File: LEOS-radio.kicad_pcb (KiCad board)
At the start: 2 copper layers, 100 x 100 mm, 20 parts, among them J1 MicroFit_1x4, J2 MicroFit_1x4, U1 MCP2562FD, U2 MCP2518FD, U3 E22-900M30S, Y1 40 MHz

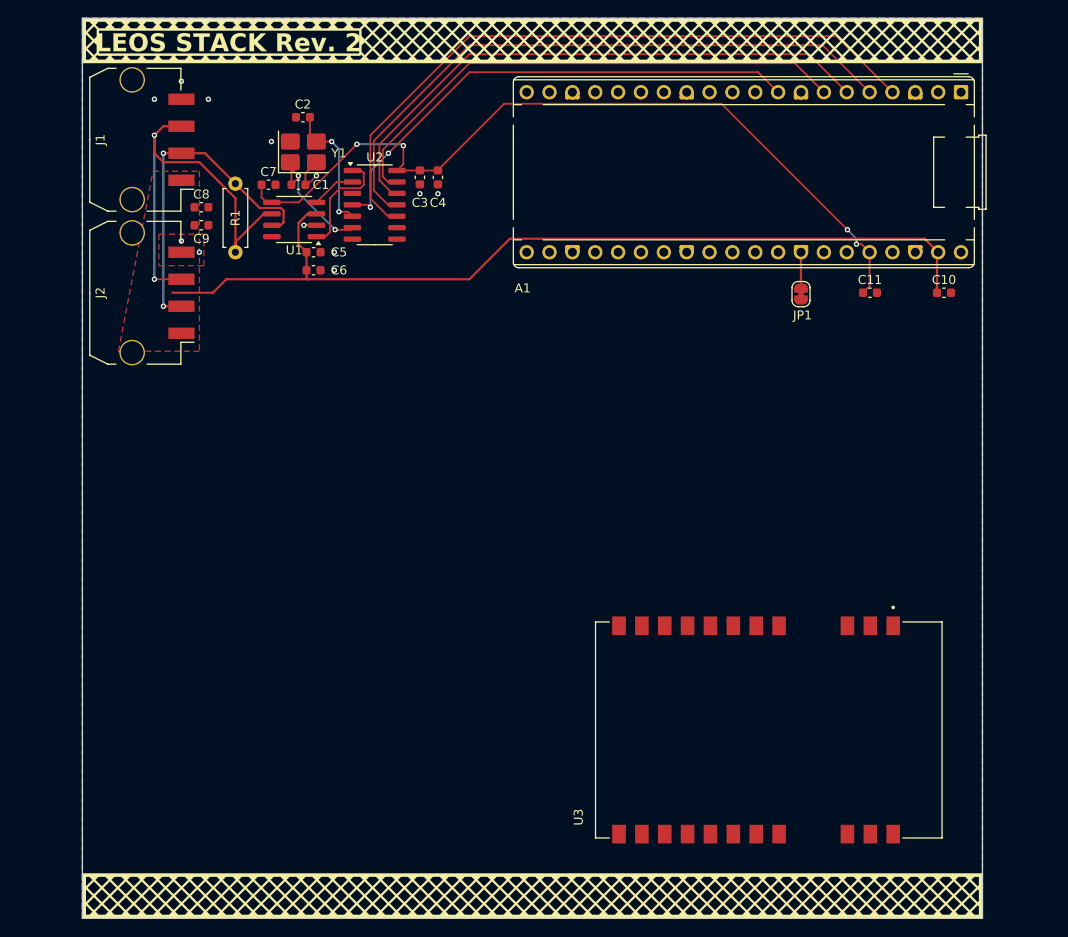
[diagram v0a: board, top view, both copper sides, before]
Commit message: v2 with dual 1W LoRa transcievers, edge-mount SMA connectors, and an all new design
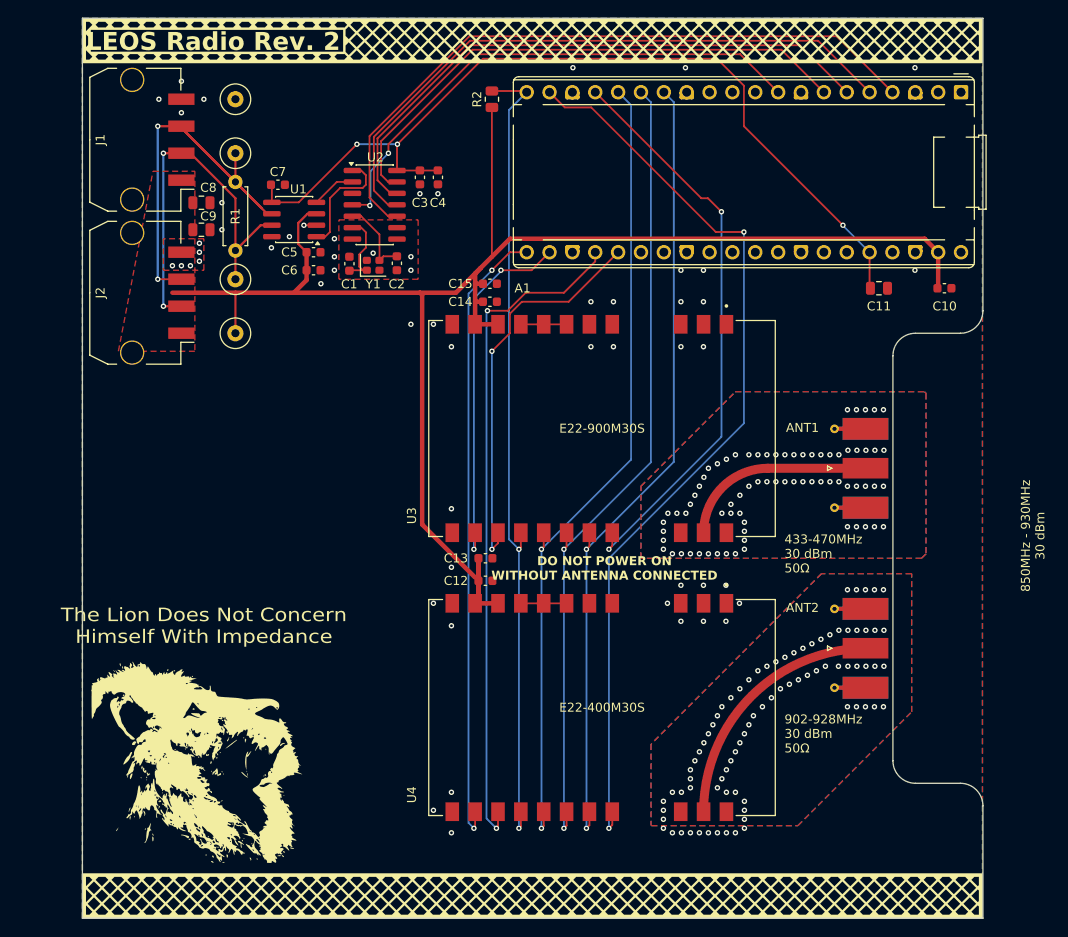
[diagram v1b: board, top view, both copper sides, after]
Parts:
- removed JP1: AGND Tie, Jumper:SolderJumper-2_P1.3mm_Bridged_RoundedPad1.0x1.5mm
- added ANT1: 900Mhz SMA, Connector_Coaxial:SMA_Molex_73251-1153_EdgeMount_Horizontal, F.Cu at (185.3, 100.0)
- added ANT2: 400MHz SMA, Connector_Coaxial:SMA_Molex_73251-1153_EdgeMount_Horizontal, F.Cu at (185.3, 120.0)
- added C12: 0.1u, Capacitor_SMD:C_0603_1608Metric, F.Cu at (144.8, 112.5)
- added C13: 1u, Capacitor_SMD:C_0603_1608Metric, F.Cu at (144.8, 110.0)
- added C14: 0.1u, Capacitor_SMD:C_0603_1608Metric, F.Cu at (145.3, 81.5)
- added C15: 1u, Capacitor_SMD:C_0603_1608Metric, F.Cu at (145.3, 79.5)
- added R2: 10k, Resistor_SMD:R_0805_2012Metric, F.Cu at (145.5, 59.0)
- added TP1: CAN-H Test Point, TestPoint:TestPoint_Loop_D2.60mm_Drill0.9mm_Beaded, F.Cu at (117.0, 79.0)
- added TP2: CAN-L Test Point, TestPoint:TestPoint_Loop_D2.60mm_Drill0.9mm_Beaded, F.Cu at (117.0, 65.0)
- added TP3: 5V Test Point, TestPoint:TestPoint_Loop_D2.60mm_Drill0.9mm_Beaded, F.Cu at (117.0, 85.0)
- added TP4: GND Test Point, TestPoint:TestPoint_Loop_D2.60mm_Drill0.9mm_Beaded, F.Cu at (117.0, 59.0)
- added U4: E22-400M30S, LEOS:XCVR_E22-900M30S, F.Cu at (157.7, 126.6)
- A1: value RaspberryPi_Pico -> RaspberryPi Pico
- C1, C2: value 12pF -> 10p
- C10, C3, C5, C7: value 0.1uF -> 0.1u
- C11: value 10uF -> 10u; footprint Capacitor_SMD:C_0603_1608Metric -> Capacitor_SMD:C_0805_2012Metric
- C4, C6: value 1uF -> 1u
- C8: value 47uF -> 22u; footprint Capacitor_SMD:C_0603_1608Metric -> Capacitor_SMD:C_0805_2012Metric
- C9: value 0.1uF -> 22u; footprint Capacitor_SMD:C_0603_1608Metric -> Capacitor_SMD:C_0805_2012Metric
- J1, J2: footprint Connector_Molex:Molex_Micro-Fit_3.0_43650-0410_1x04-1MP_P3.00mm_Horizontal_PnP -> LEOS:Molex_MicroFit3.0_43650-0410_1x04_Horizontal
- R1: value 120R -> 120
- Y1: footprint Crystal:Crystal_SMD_3225-4Pin_3.2x2.5mm_HandSoldering -> Crystal:Crystal_SMD_2016-4Pin_2.0x1.6mm
- moved U3 38.3 mm to (157.7, 95.6)
- moved C2 19.3 mm to (134.9, 77.2), turned to 90 degrees
- moved Y1 14.8 mm to (132.3, 77.5)
- moved C1 10.4 mm to (129.7, 77.3), turned to -90 degrees
- moved R1 7.81 mm to (117.0, 68.2), turned to -90 degrees
- moved C11 1.12 mm to (188.5, 80.0)
- moved C7 1.04 mm to (121.7, 68.5)
- moved C10 0.50 mm to (195.8, 80.0)
- moved C8 0.50 mm to (113.2, 70.5)
- moved C9 0.50 mm to (113.2, 73.5)
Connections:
- net /CAN+ renamed /CANbus/CAN+
- net /CAN- renamed /CANbus/CAN-
- net /CAN_CS renamed /CANbus/CS
- net /CAN_INT renamed /CANbus/INT
- net /CAN_MISO renamed /CANbus/MISO
- net /CAN_MOSI renamed /CANbus/MOSI
- net /CAN_SCK renamed /CANbus/SCK
- net /OSC2 renamed /CANbus/OSC2
- net /RXCAN renamed Net-(U1-RXD)
- net /TXCAN renamed Net-(U1-TXD)
- A1 pad 1: UART0_TX -> unconnected-(A1-GPIO0-Pad1)
- A1 pad 10: GP7 -> unconnected-(A1-GPIO7-Pad10)
- A1 pad 11: I2C0_SDA -> unconnected-(A1-GPIO8-Pad11)
- A1 pad 12: I2C0_SCL -> unconnected-(A1-GPIO9-Pad12)
- A1 pad 14: GP10 -> /RF/SCK
- A1 pad 15: GP11 -> /RF/MOSI
- A1 pad 16: GP12 -> /RF/MISO
- A1 pad 17: GP13 -> /RF/CS0
- A1 pad 19: GP14 -> /RF/CS1
- A1 pad 2: UART0_RX -> unconnected-(A1-GPIO1-Pad2)
- A1 pad 20: GP15 -> /RF/nRESET
- A1 pad 21: GP16 -> /RF/INT1
- A1 pad 22: GP17 -> /RF/INT0
- A1 pad 24: GP18 -> /RF/BUSY1
- A1 pad 25: GP19 -> /RF/BUSY0
- A1 pad 26: GP20 -> unconnected-(A1-GPIO20-Pad26)
- A1 pad 27: GP21 -> unconnected-(A1-GPIO21-Pad27)
- A1 pad 29: GP22 -> unconnected-(A1-GPIO22-Pad29)
- A1 pad 30: RUN -> unconnected-(A1-RUN-Pad30)
- A1 pad 31: ADC0 -> unconnected-(A1-GPIO26_ADC0-Pad31)
- A1 pad 32: ADC1 -> unconnected-(A1-GPIO27_ADC1-Pad32)
- A1 pad 33: Net-(A1-AGND) -> unconnected-(A1-AGND-Pad33)
- A1 pad 34: ADC2 -> unconnected-(A1-GPIO28_ADC2-Pad34)
- C1 pad 1: /OSC1 -> GND
- C1 pad 2: GND -> /CANbus/OSC1
- U2 pad 6: /OSC1 -> /CANbus/OSC1
- U3 pad 10: VCC -> +5V
- U3 pad 13: unconnected-(U3-DIO1-Pad13) -> /RF/INT0
- U3 pad 14: unconnected-(U3-BUSY-Pad14) -> /RF/BUSY0
- U3 pad 15: unconnected-(U3-~{RST}-Pad15) -> /RF/nRESET
- U3 pad 16: unconnected-(U3-MISO-Pad16) -> /RF/MISO
- U3 pad 17: unconnected-(U3-MOSI-Pad17) -> /RF/MOSI
- U3 pad 18: unconnected-(U3-SCK-Pad18) -> /RF/SCK
- U3 pad 19: unconnected-(U3-NSS-Pad19) -> /RF/CS0
- U3 pad 21: unconnected-(U3-ANT-Pad21) -> /RF/RF_900MHz
- U3 pad 6: unconnected-(U3-RXEN-Pad6) -> Net-(U3-DIO2)
- U3 pad 7: unconnected-(U3-TXEN-Pad7) -> Net-(U3-DIO2)
- U3 pad 8: unconnected-(U3-DIO2-Pad8) -> Net-(U3-DIO2)
- U3 pad 9: VCC -> +5V
- Y1 pad 1: /OSC1 -> /CANbus/OSC1
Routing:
- net /RF/CS1: track 0.00 -> 102.5 mm, vias 0 -> 2
- net /RF/nRESET: track 0.00 -> 90.6 mm, vias 0 -> 2
- net /RF/MISO: track 0.00 -> 90.4 mm, vias 0 -> 2
- net /RF/SCK: track 0.00 -> 90.2 mm, vias 0 -> 2
- net /RF/MOSI: track 0.00 -> 90.2 mm, vias 0 -> 2
- net +5V: track 101.8 -> 181.1 mm
- net /RF/BUSY1: track 0.00 -> 75.2 mm, vias 0 -> 2
- net /RF/INT1: track 0.00 -> 69.9 mm, vias 0 -> 2
- net /RF/CS0: track 0.00 -> 64.2 mm, vias 0 -> 2
- net /RF/BUSY0: track 0.00 -> 44.0 mm, vias 0 -> 2
- net /RF/INT0: track 0.00 -> 40.4 mm, vias 0 -> 2
- net /RF/RF_400MHz: track 0.00 -> 27.8 mm
- net /RF/RF_900MHz: track 0.00 -> 22.5 mm
- net /OSC1: track 15.4 -> 0.00 mm, vias 2 -> 0
- net /CANbus/OSC1: track 0.00 -> 8.74 mm
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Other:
- board size 100 x 100 mm -> 100.1 x 100 mm
- board text added: "02/18/2026"
- board text added: "433-470MHz 30 dBm 50Ω"
- board text added: "5V"
- board text added: "850MHz - 930MHz 30 dBm"
- board text added: "902-928MHz 30 dBm 50Ω"
- board text added: "CAN-H"
- board text added: "CAN-L"
- board text added: "DO NOT POWER ON WITHOUT ANTENNA CONNECTED"
- board text added: "GND"
- board text added: "LEOS Radio Rev. 2"
- board text added: "The Lion Does Not Concern Himself With Impedance"
- board text removed: "LEOS STACK Rev. 2"

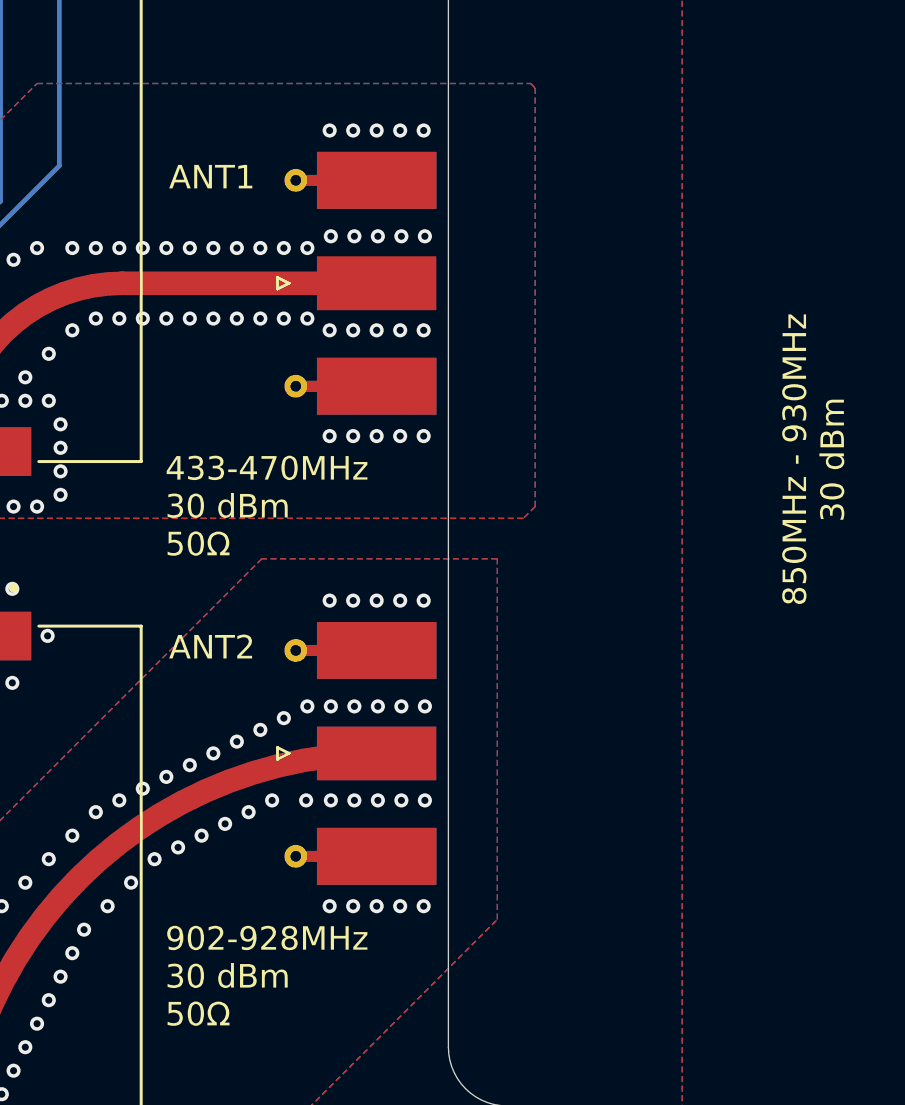
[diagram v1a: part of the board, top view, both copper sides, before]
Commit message: Fix backwards ANT labels and increase font size
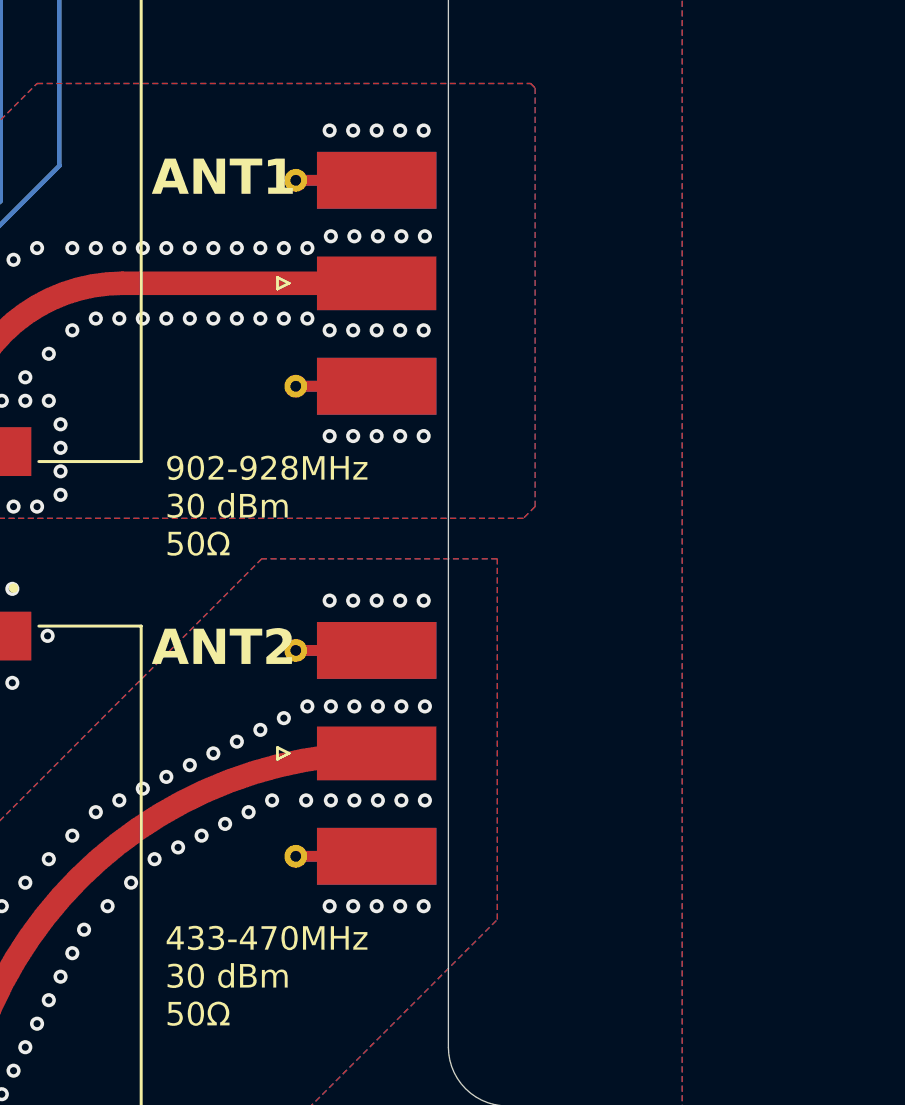
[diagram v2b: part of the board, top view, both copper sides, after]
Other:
- board text removed: "850MHz - 930MHz 30 dBm"
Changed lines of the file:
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@@
 		(tags "sma edge")
 		(property "Reference" "ANT1"
-			(at 5.28 4.5 0)
+			(at 4.78 4.5 0)
 			(layer "F.SilkS")
 			(effects
 				(font
-					(size 1 1)
-					(thickness 0.15)
+					(size 1.5 1.5)
+					(thickness 0.3)
+					(bold yes)
 				)
 			)
@@
 		(tags "sma edge")
 		(property "Reference" "ANT2"
-			(at 5.28 4.5 0)
+			(at 4.78 4.5 0)
 			(layer "F.SilkS")
 			(effects
 				(font
-					(size 1 1)
-					(thickness 0.15)
+					(size 1.5 1.5)
+					(thickness 0.3)
+					(bold yes)
 				)
 			)
@@
 	)
 	(gr_text "902-928MHz\n30 dBm\n50Ω"
-		(at 178 129.5 0)
+		(at 178 109.5 0)
 		(layer "F.SilkS")
 		(effects
@@
 		)
 	)
-	(gr_text "850MHz - 930MHz\n30 dBm"
-		(at 207 107.5 90)
-		(layer "F.SilkS")
-		(effects
-			(font
-				(size 1 1)
-				(thickness 0.15)
-			)
-			(justify bottom)
-		)
-	)
 	(gr_text "DO NOT POWER ON \nWITHOUT ANTENNA CONNECTED"
 		(at 158 112.5 0)
@@
 	)
 	(gr_text "433-470MHz\n30 dBm\n50Ω"
-		(at 178 109.5 0)
+		(at 178 129.5 0)
 		(layer "F.SilkS")
 		(effects
